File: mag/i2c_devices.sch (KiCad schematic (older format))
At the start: 5 parts

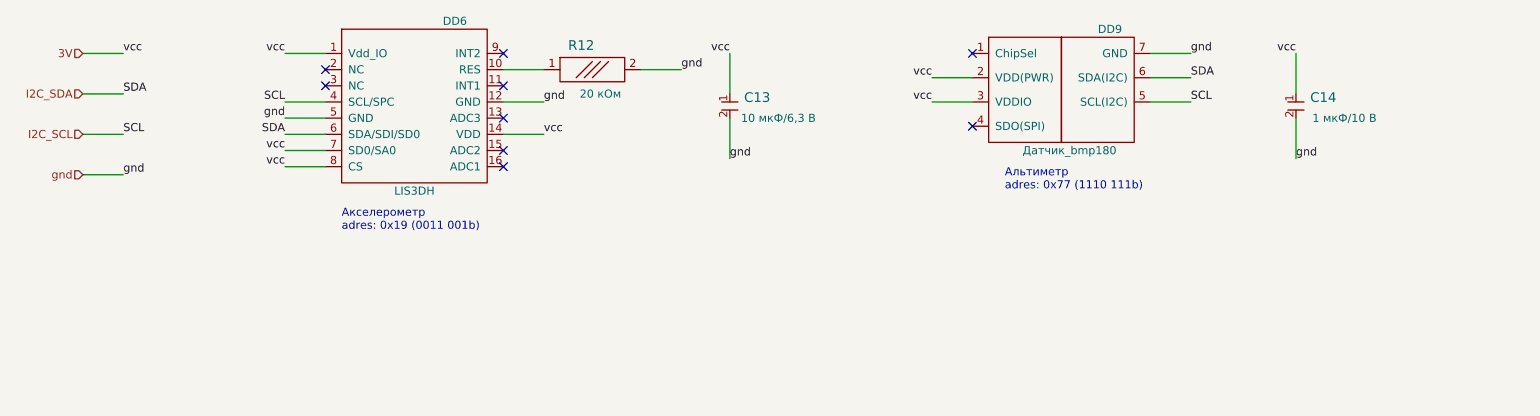
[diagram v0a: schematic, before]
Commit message: закончена около-боевая разводка, на плате оставлены штыревые разъемы
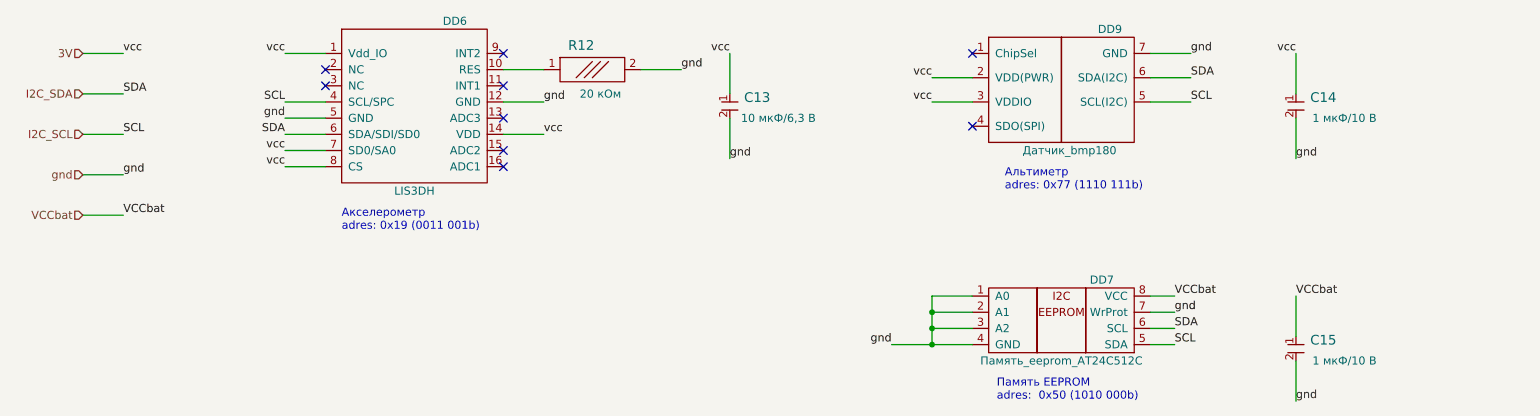
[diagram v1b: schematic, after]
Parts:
- added C15: Конденсатор_керамический, N_RLC:Конденсатор_SMD_0603, symbol elements:Конденсатор_керамический
- added DD7: Память_eeprom_AT24C512C, N_DD:SO-8, symbol elements:Память_eeprom_AT24C512C
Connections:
- net I2C_SCL: now also DD7.5 (SDA)
- net I2C_SDA: now also DD7.6 (SCL)
- net gnd: now also C15.2, DD7.1 (A0), DD7.2 (A1), DD7.3 (A2), DD7.4 (GND), DD7.7 (WrProt)
- new net VCCbat: C15.1, DD7.8 (VCC)
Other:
- note added: "Память EEPROM\nadres: 0x50 (1010 000b)"
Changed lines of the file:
@@
 	0    1    1    0
 $EndComp
+$Comp
+L elements:Память_eeprom_AT24C512C DD7
+U 1 1 5D8F9F5D
+P 7600 4000
+F 0 "DD7" H 8300 4100 50  0000 C CNN
+F 1 "Память_eeprom_AT24C512C" H 8050 3600 50  0000 C CNN
+F 2 "N_DD:SO-8" H 7500 4000 50  0001 C CNN
+F 3 "" H 7500 4000 50  0001 C CNN
+	1    7600 4000
+	1    0    0    -1
+$EndComp
+Text Notes 7650 4650 0    50   ~ 0
+Память EEPROM\nadres:  0x50 (1010 000b)
+Text Label 8750 4300 0    50   ~ 0
+SCL
+Text Label 8750 4200 0    50   ~ 0
+SDA
+Wire Wire Line
+	8750 4200 8600 4200
+Wire Wire Line
+	8600 4300 8750 4300
+Wire Wire Line
+	8750 4000 8600 4000
+Text Label 8750 4100 0    50   ~ 0
+gnd
+Wire Wire Line
+	7500 4000 7250 4000
+Wire Wire Line
+	7500 4100 7250 4100
+Wire Wire Line
+	7500 4200 7250 4200
+Text Label 7000 4300 2    50   ~ 0
+gnd
+Wire Wire Line
+	7000 4300 7250 4300
+Wire Wire Line
+	8750 4100 8600 4100
+Wire Wire Line
+	7250 4300 7250 4200
+Connection ~ 7250 4300
+Wire Wire Line
+	7250 4300 7500 4300
+Connection ~ 7250 4100
+Wire Wire Line
+	7250 4100 7250 4000
+Connection ~ 7250 4200
+Wire Wire Line
+	7250 4200 7250 4100
+Wire Wire Line
+	9500 4000 9500 4250
+Wire Wire Line
+	9500 4400 9500 4650
+Text Label 9500 4650 0    50   ~ 0
+gnd
+$Comp
+L elements:Конденсатор_керамический C?
+U 1 1 5D903FED
+P 9500 4300
+AR Path="/5D903FED" Ref="C?"  Part="1"
+AR Path="/5D924959/5D903FED" Ref="C?"  Part="1"
+AR Path="/5DB88CD1/5D903FED" Ref="C?"  Part="1"
+AR Path="/5DCA4D45/5D903FED" Ref="C15"  Part="1"
+F 0 "C15" V 9472 4388 60  0000 L CNN
+F 1 "Конденсатор_керамический" V 9578 4388 60  0001 L CNN
+F 2 "N_RLC:Конденсатор_SMD_0603" H 9500 4300 60  0001 C CNN
+F 3 "" H 9500 4300 60  0001 C CNN
+F 4 "1 мкФ/10 В" V 9600 4600 50  0000 C CNN "Номинал"
+F 5 "С111" H 9500 4300 50  0001 C CNN "УГО"
+	1    9500 4300
+	0    1    1    0
+$EndComp
+Text HLabel 2000 3500 0    50   Input ~ 0
+VCCbat
+Wire Wire Line
+	2000 3500 2250 3500
+Text Label 2250 3500 0    50   ~ 0
+VCCbat
+Text Label 8750 4000 0    50   ~ 0
+VCCbat
+Text Label 9500 4000 0    50   ~ 0
+VCCbat
 $EndSCHEMATC

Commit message: сформированны файлы для заказа
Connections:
- net I2C_SCL: now also DD7.6 (SCL); no longer DD7.5 (SDA)
- net I2C_SDA: now also DD7.5 (SDA); no longer DD7.6 (SCL)
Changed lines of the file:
@@
 Text Notes 7650 4650 0    50   ~ 0
 Память EEPROM\nadres:  0x50 (1010 000b)
+Text Label 8750 4200 0    50   ~ 0
+SCL
 Text Label 8750 4300 0    50   ~ 0
-SCL
-Text Label 8750 4200 0    50   ~ 0
 SDA
 Wire Wire Line

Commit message: библиотека bmp180, замечания к схеме
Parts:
- C13, C14, C15: symbol elements:Конденсатор_керамический -> mag-rescue:Конденсатор_керамический-elements
- DD6: symbol elements:LIS3DH -> mag-rescue:LIS3DH-elements
- DD7: symbol elements:Память_eeprom_AT24C512C -> mag-rescue:Память_eeprom_AT24C512C-elements
- DD9: symbol elements:Датчик_bmp180 -> mag-rescue:Датчик_bmp180-elements
- R12: symbol elements:Резистор_0,065Вт -> mag-rescue:Резистор_0,065Вт-elements
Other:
- note added: "отодвинуть от G2"
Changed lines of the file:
@@
 EESchema Schematic File Version 4
 LIBS:mag-cache
-EELAYER 29 0
+EELAYER 30 0
 EELAYER END
 $Descr A4 11693 8268
@@
 I2C_SCL
 $Comp
-L elements:LIS3DH DD?
+L mag-rescue:LIS3DH-elements DD?
 U 1 1 5DCBE002
 P 3500 2500
@@
 vcc
 $Comp
-L elements:Конденсатор_керамический C?
+L mag-rescue:Конденсатор_керамический-elements C?
 U 1 1 5DCF31B7
 P 6000 2800
@@
 	4600 2600 4850 2600
 $Comp
-L elements:Резистор_0,065Вт R?
+L mag-rescue:Резистор_0,065Вт-elements R?
 U 1 1 5DD39505
 P 5150 2600
@@
 vcc
 $Comp
-L elements:Датчик_bmp180 DD9
+L mag-rescue:Датчик_bmp180-elements DD9
 U 1 1 5D8E78D8
 P 7500 2500
@@
 gnd
 $Comp
-L elements:Конденсатор_керамический C?
+L mag-rescue:Конденсатор_керамический-elements C?
 U 1 1 5D8ED9F7
 P 9500 2800
@@
 $EndComp
 $Comp
-L elements:Память_eeprom_AT24C512C DD7
+L mag-rescue:Память_eeprom_AT24C512C-elements DD7
 U 1 1 5D8F9F5D
 P 7600 4000
@@
 gnd
 $Comp
-L elements:Конденсатор_керамический C?
+L mag-rescue:Конденсатор_керамический-elements C?
 U 1 1 5D903FED
 P 9500 4300
@@
 Text Label 9500 4000 0    50   ~ 0
 VCCbat
+Text Notes 9750 4600 0    50   ~ 0
+отодвинуть от G2
 $EndSCHEMATC
